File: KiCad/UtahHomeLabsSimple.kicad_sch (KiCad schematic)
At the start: 4 parts, among them X1 SAINTCON-Minibadge-Simple

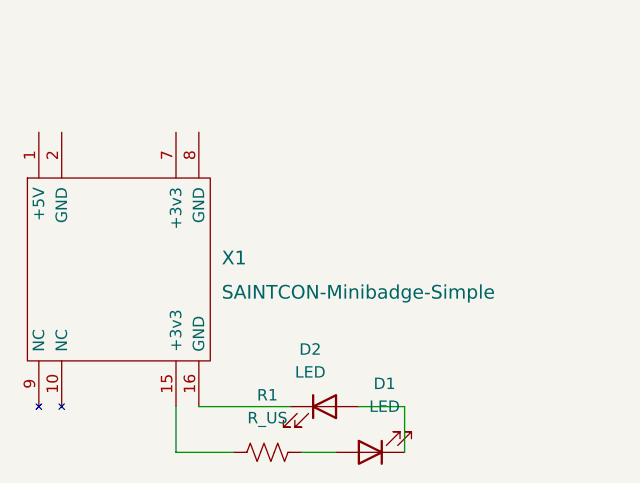
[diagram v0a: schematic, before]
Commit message: Updates
Updated Schema to Parallel
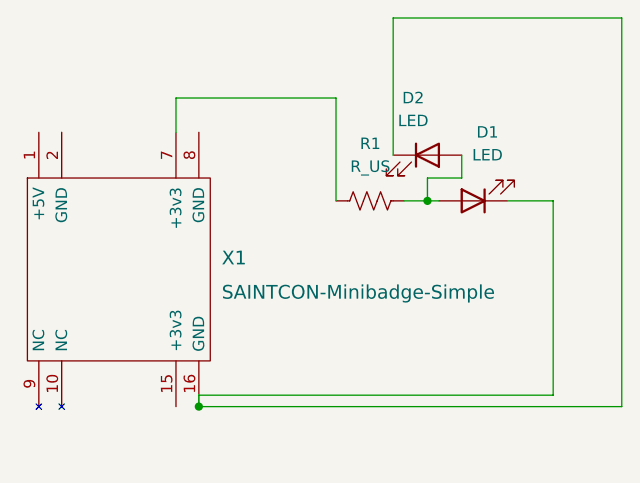
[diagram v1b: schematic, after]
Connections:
- net at D2.1 (K), X1.16 (GND): now also D1.1 (K)
- net at D2.2 (A): now also D1.2 (A), R1.2; no longer D1.1 (K)
- net at R1.1: now also X1.7 (+3v3); no longer X1.15 (+3v3)
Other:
- moved on the sheet: D1, D2, R1
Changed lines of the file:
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@@
 (kicad_sch (version 20211123) (generator eeschema)
   (paper "A4")
-  (wire (pts (xy 139.7 111.76) (xy 139.7 116.84))
+  (junction (at 167.64 88.9) (diameter 0) (color 0 0 0 0)
+  )
+  (junction (at 142.24 111.76) (diameter 0) (color 0 0 0 0)
+  )
+  (wire (pts (xy 163.83 83.82) (xy 163.83 68.58))
     (stroke (width 0) (type default) (color 0 0 0 0))
   )
-  (wire (pts (xy 165.1 116.84) (xy 165.1 111.76))
+  (wire (pts (xy 139.7 77.47) (xy 157.48 77.47))
     (stroke (width 0) (type default) (color 0 0 0 0))
   )
-  (wire (pts (xy 142.24 111.76) (xy 152.4 111.76))
+  (wire (pts (xy 142.24 110.49) (xy 142.24 111.76))
     (stroke (width 0) (type default) (color 0 0 0 0))
   )
-  (wire (pts (xy 160.02 111.76) (xy 165.1 111.76))
+  (wire (pts (xy 189.23 68.58) (xy 189.23 111.76))
     (stroke (width 0) (type default) (color 0 0 0 0))
   )
-  (wire (pts (xy 153.67 116.84) (xy 157.48 116.84))
+  (wire (pts (xy 167.64 88.9) (xy 168.91 88.9))
     (stroke (width 0) (type default) (color 0 0 0 0))
   )
-  (wire (pts (xy 139.7 116.84) (xy 146.05 116.84))
+  (wire (pts (xy 139.7 81.28) (xy 139.7 77.47))
     (stroke (width 0) (type default) (color 0 0 0 0))
   )
-  (symbol (lib_id "Device:LED") (at 156.21 111.76 0) (unit 1)
+  (wire (pts (xy 142.24 110.49) (xy 181.61 110.49))
+    (stroke (width 0) (type default) (color 0 0 0 0))
+  )
+  (wire (pts (xy 157.48 77.47) (xy 157.48 88.9))
+    (stroke (width 0) (type default) (color 0 0 0 0))
+  )
+  (wire (pts (xy 167.64 88.9) (xy 167.64 86.36))
+    (stroke (width 0) (type default) (color 0 0 0 0))
+  )
+  (wire (pts (xy 142.24 111.76) (xy 189.23 111.76))
+    (stroke (width 0) (type default) (color 0 0 0 0))
+  )
+  (wire (pts (xy 165.1 88.9) (xy 167.64 88.9))
+    (stroke (width 0) (type default) (color 0 0 0 0))
+  )
+  (wire (pts (xy 163.83 68.58) (xy 189.23 68.58))
+    (stroke (width 0) (type default) (color 0 0 0 0))
+  )
+  (wire (pts (xy 181.61 88.9) (xy 181.61 110.49))
+    (stroke (width 0) (type default) (color 0 0 0 0))
+  )
+  (wire (pts (xy 176.53 88.9) (xy 181.61 88.9))
+    (stroke (width 0) (type default) (color 0 0 0 0))
+  )
+  (wire (pts (xy 171.45 86.36) (xy 171.45 83.82))
+    (stroke (width 0) (type default) (color 0 0 0 0))
+  )
+  (wire (pts (xy 167.64 86.36) (xy 171.45 86.36))
+    (stroke (width 0) (type default) (color 0 0 0 0))
+  )
+  (symbol (lib_id "Device:LED") (at 167.64 83.82 0) (unit 1)
     (in_bom yes) (on_board yes) (fields_autoplaced)
-    (property "Reference" "D2" (id 0) (at 154.6225 105.41 0))
-    (property "Value" "LED" (id 1) (at 154.6225 107.95 0))
-    (property "Footprint" "LED_SMD:LED_1206_3216Metric_Pad1.42x1.75mm_HandSolder" (id 2) (at 156.21 111.76 0)
+    (property "Reference" "D2" (id 0) (at 166.0525 77.47 0))
+    (property "Value" "LED" (id 1) (at 166.0525 80.01 0))
+    (property "Footprint" "LED_SMD:LED_1206_3216Metric_Pad1.42x1.75mm_HandSolder" (id 2) (at 167.64 83.82 0)
       (effects (font (size 1.27 1.27)) hide)
     )
-    (property "Datasheet" "~" (id 3) (at 156.21 111.76 0)
+    (property "Datasheet" "~" (id 3) (at 167.64 83.82 0)
       (effects (font (size 1.27 1.27)) hide)
     )
@@
     (pin "2")
   )
-  (symbol (lib_id "Device:LED") (at 161.29 116.84 180) (unit 1)
+  (symbol (lib_id "Device:LED") (at 172.72 88.9 180) (unit 1)
     (in_bom yes) (on_board yes) (fields_autoplaced)
-    (property "Reference" "D1" (id 0) (at 162.8775 109.22 0))
-    (property "Value" "LED" (id 1) (at 162.8775 111.76 0))
-    (property "Footprint" "LED_SMD:LED_1206_3216Metric_Pad1.42x1.75mm_HandSolder" (id 2) (at 161.29 116.84 0)
+    (property "Reference" "D1" (id 0) (at 174.3075 81.28 0))
+    (property "Value" "LED" (id 1) (at 174.3075 83.82 0))
+    (property "Footprint" "LED_SMD:LED_1206_3216Metric_Pad1.42x1.75mm_HandSolder" (id 2) (at 172.72 88.9 0)
       (effects (font (size 1.27 1.27)) hide)
     )
-    (property "Datasheet" "~" (id 3) (at 161.29 116.84 0)
+    (property "Datasheet" "~" (id 3) (at 172.72 88.9 0)
       (effects (font (size 1.27 1.27)) hide)
     )
@@
     (pin "2")
   )
-  (symbol (lib_id "Device:R_US") (at 149.86 116.84 90) (unit 1)
+  (symbol (lib_id "Device:R_US") (at 161.29 88.9 90) (unit 1)
     (in_bom yes) (on_board yes) (fields_autoplaced)
-    (property "Reference" "R1" (id 0) (at 149.86 110.49 90))
-    (property "Value" "R_US" (id 1) (at 149.86 113.03 90))
-    (property "Footprint" "Resistor_SMD:R_1206_3216Metric_Pad1.30x1.75mm_HandSolder" (id 2) (at 150.114 115.824 90)
+    (property "Reference" "R1" (id 0) (at 161.29 82.55 90))
+    (property "Value" "R_US" (id 1) (at 161.29 85.09 90))
+    (property "Footprint" "Resistor_SMD:R_1206_3216Metric_Pad1.30x1.75mm_HandSolder" (id 2) (at 161.544 87.884 90)
       (effects (font (size 1.27 1.27)) hide)
     )
-    (property "Datasheet" "~" (id 3) (at 149.86 116.84 0)
+    (property "Datasheet" "~" (id 3) (at 161.29 88.9 0)
       (effects (font (size 1.27 1.27)) hide)
     )

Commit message: Updated Graphics
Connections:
- net at D2.1 (K), X1.16 (GND): no longer D1.1 (K)
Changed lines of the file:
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@@
-    (stroke (width 0) (type default) (color 0 0 0 0))
-  )
-  (wire (pts (xy 142.24 110.49) (xy 181.61 110.49))
     (stroke (width 0) (type default) (color 0 0 0 0))
   )
@@
     (stroke (width 0) (type default) (color 0 0 0 0))
   )
-  (wire (pts (xy 181.61 88.9) (xy 181.61 110.49))
-    (stroke (width 0) (type default) (color 0 0 0 0))
-  )
-  (wire (pts (xy 176.53 88.9) (xy 181.61 88.9))
-    (stroke (width 0) (type default) (color 0 0 0 0))
-  )
